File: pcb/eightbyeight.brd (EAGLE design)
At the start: 60 x 60 mm, 137 parts, among them CON1 USB_MICROSMT+THRUHULE, Q1 16MHz, SW1 SWITCH_SPDT, SW2 BRIGHTNESS, U1 MK20DN64VFM5, U10 FDG6316P, U11 FDG6316P, U12 FDG6316P, U2 ICN2026, U3 74138, U4 ICN2026, U5 MIC5219 3.3V, U6 ESP_WROOM_02, U8 MMA8653FC, U9 FDG6316P

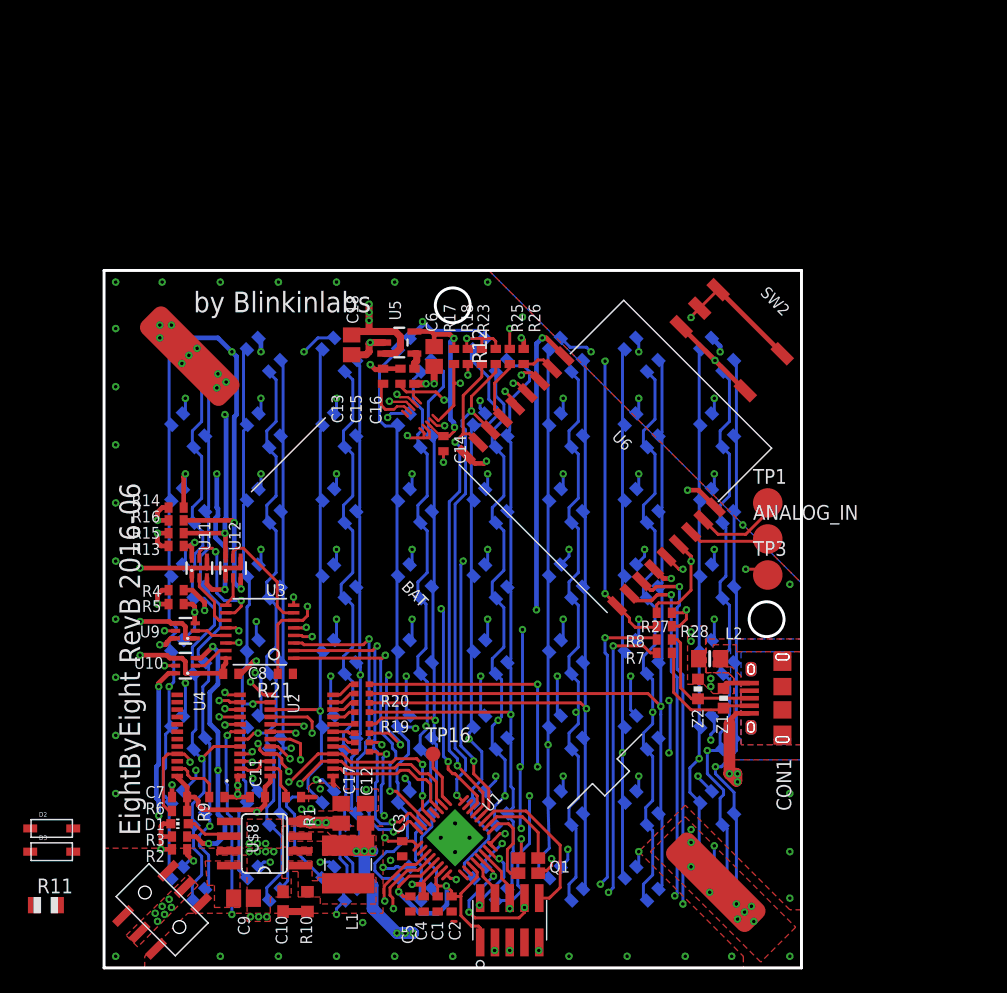
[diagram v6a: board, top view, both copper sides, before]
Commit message: Finish placing power diodes and clear DRC errors
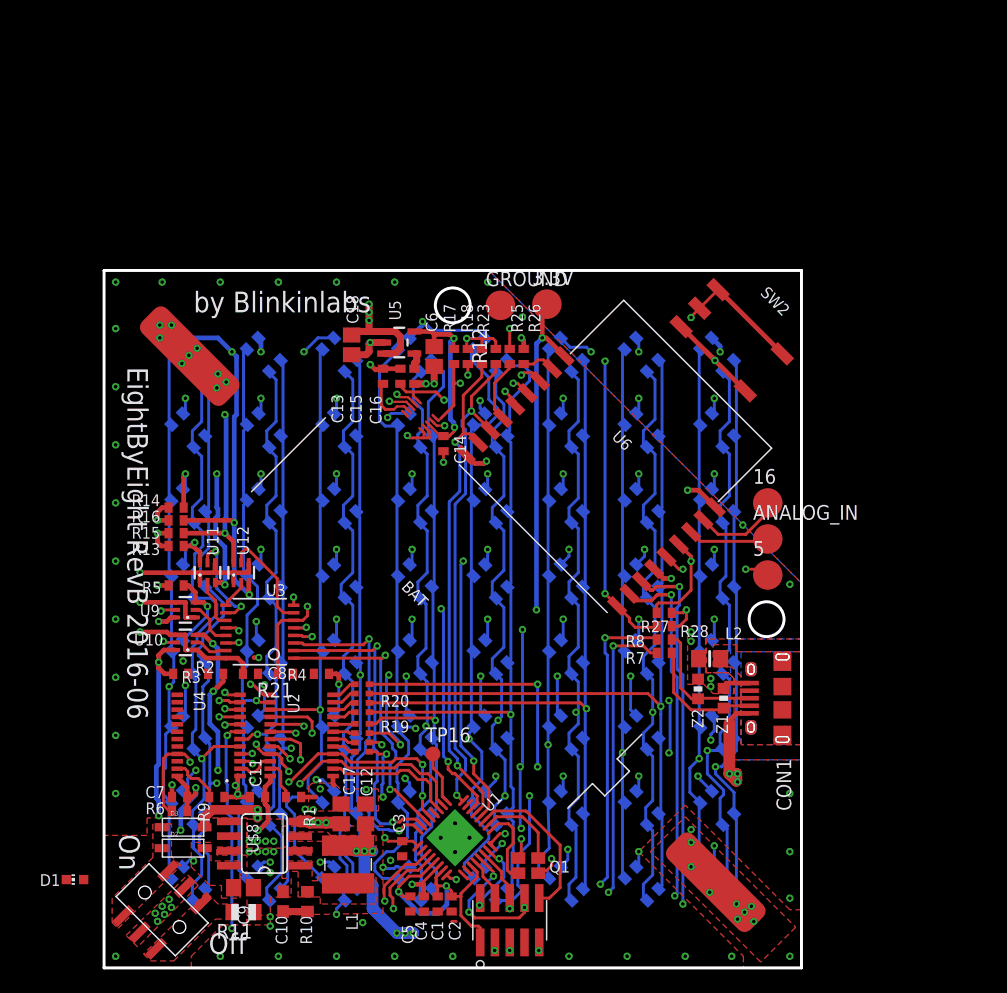
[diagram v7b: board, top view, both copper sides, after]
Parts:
- added 3.3V, GROUND: PTR1B2,54, testpad:B2,54
- moved R11 17.0 mm to (12.0, 4.80), turned to 180 degrees
- moved R2 15.1 mm to (6.60, 25.3), turned to 180 degrees
- moved R4 14.4 mm to (18.7, 25.3)
- moved R3 14.3 mm to (9.60, 25.3)
- moved D3 11.5 mm to (6.80, 12.1)
- moved D2 11.4 mm to (6.80, 10.3)
- moved D1 10.2 mm to (-2.50, 7.60)
- moved U10 2.00 mm to (7.00, 28.0)
- moved U9 1.80 mm to (7.00, 30.8)
- moved C8 1.70 mm to (12.6, 25.3)
- moved R5 1.60 mm to (6.20, 32.9)
- moved C9 0.90 mm to (12.0, 6.90)
- moved U11 0.81 mm to (8.90, 34.0)
- moved U12 0.81 mm to (11.8, 34.0)
- moved C12 0.05 mm to (22.5, 13.2)
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- renumbered TP1 to 16, TP3 to 5
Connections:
- net ESP_EXP_1 renamed EXP_GPIO5
- net ESP_EXP_2 renamed ESP_GPIO16
- net N$1 renamed +5V_SWITCH
- net N$4 renamed +5V_BLEED
- net +3V3: now also 3.3V.TP
- net GND: now also GROUND.TP
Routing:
- net USB_5V: track 53.6 -> 65.0 mm, vias 6 -> 8
- net 1ROW2: track 94.2 -> 85.1 mm, vias 10 -> 9
- net 1ROW1: track 82.1 -> 74.3 mm
- net ARM_3V3: track 62.0 -> 68.4 mm, vias 4 -> 6
- net GND: track 99.0 -> 92.7 mm, vias 90 -> 91
- net CHARGE: track 3.99 -> 0.04 mm
- net +3V3: track 79.0 -> 82.3 mm
- net 1ROW0: track 82.8 -> 85.8 mm
- net RCOL0: track 74.6 -> 72.1 mm
- net 1ROW5: track 72.3 -> 70.5 mm
- net LED_S3: track 8.57 -> 9.92 mm
- net GCOL2: track 78.1 -> 79.4 mm
- net LED_S5: track 10.2 -> 8.95 mm
- net LED_S2: track 2.80 -> 4.04 mm
- net 1ROW3: track 63.7 -> 64.8 mm
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- added copper zone on layer 1, net +5V_BLEED
- added copper zone on layer 1, net +5V_SWITCH
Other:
- board text added: "Off"
- board text added: "On"

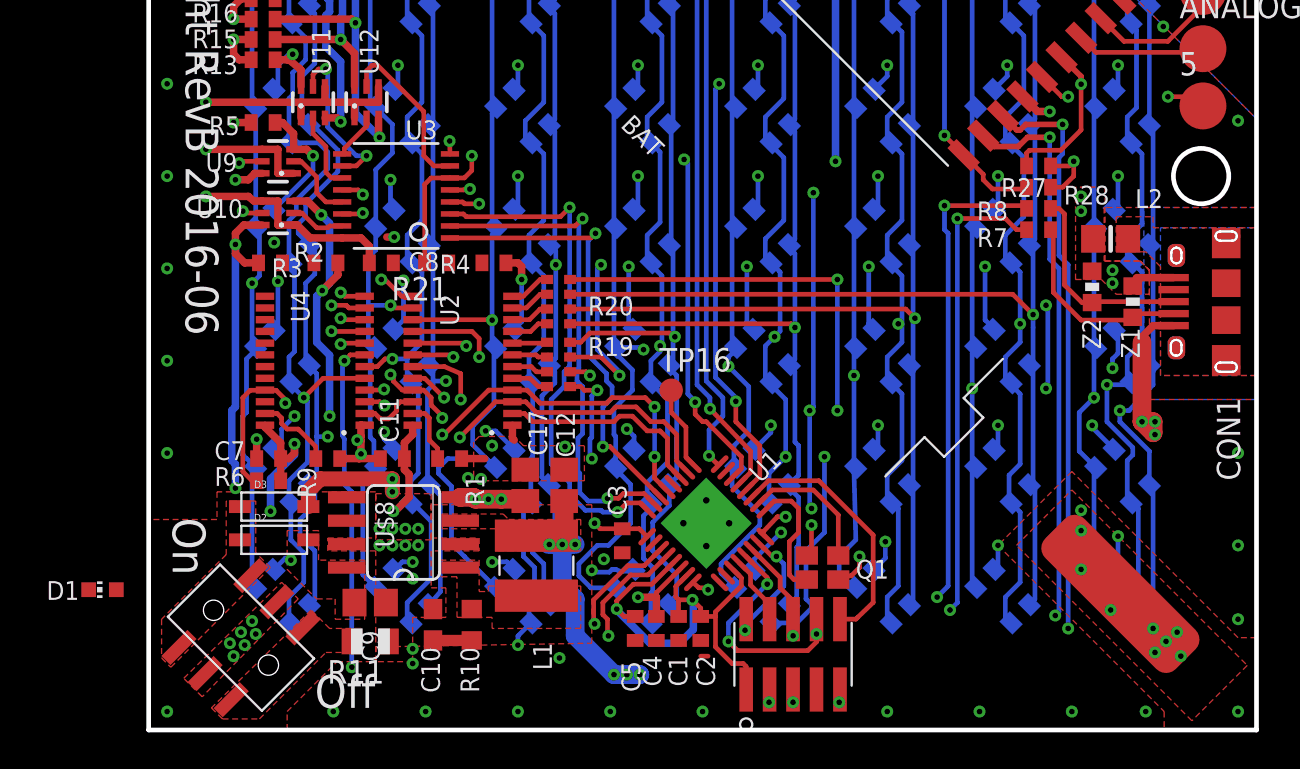
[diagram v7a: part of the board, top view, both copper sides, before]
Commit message: Add discharge LED, finish board routing!
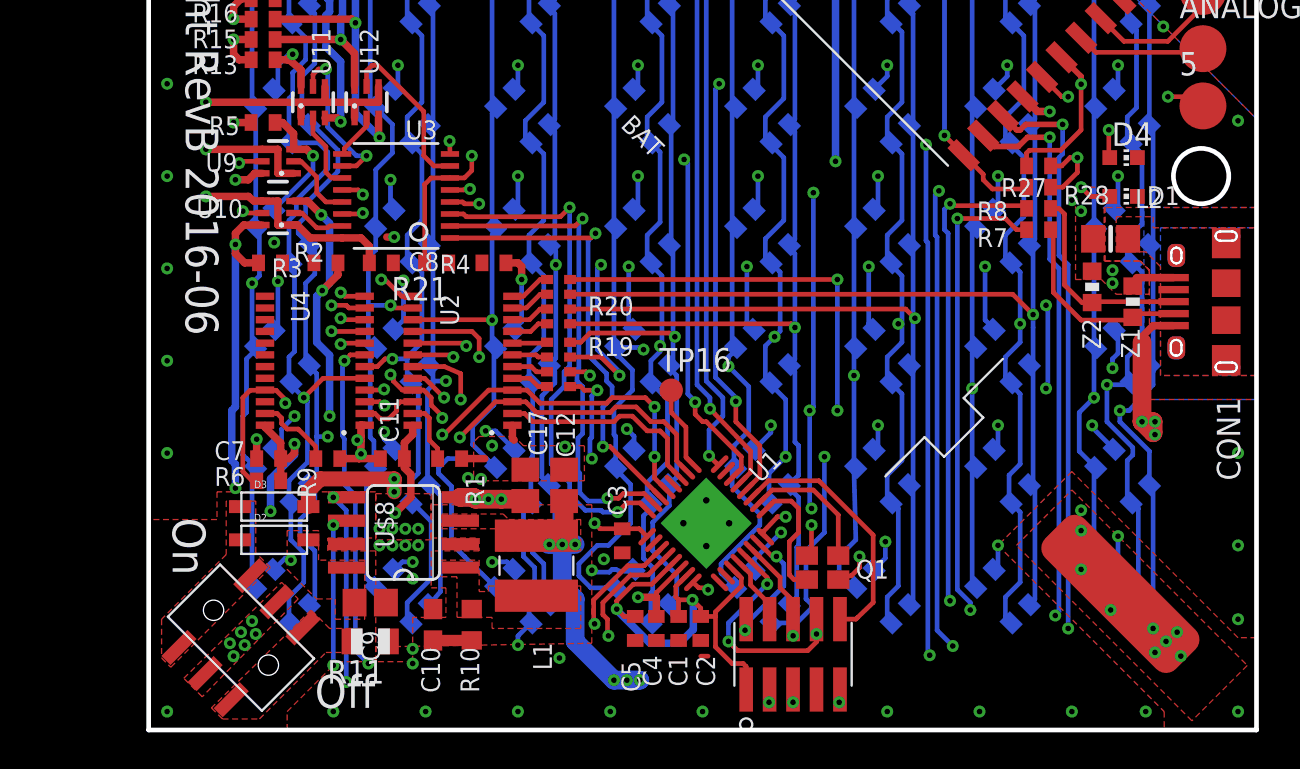
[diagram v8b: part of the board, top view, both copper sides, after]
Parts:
- added D4: BLUE, adafruit:CHIP-LED0603
- moved D1 59.3 mm to (52.8, 28.9), turned to 270 degrees
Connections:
- new net DISCHARGE: D4.A, U$8.5
- net GND: now also D4.C
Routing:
- net DISCHARGE: track 0.00 -> 83.1 mm, vias 0 -> 5
- net CHARGE: track 0.04 -> 77.8 mm, vias 0 -> 5
- net USB_D-: track 51.0 -> 52.3 mm
- net +3V3: track 82.3 -> 83.2 mm
- net GCOL2: track 79.4 -> 78.6 mm
- net USB_D+: track 51.7 -> 52.2 mm
